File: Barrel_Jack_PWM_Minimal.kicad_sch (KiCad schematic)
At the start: 18 parts, among them J28 Barrel_Jack_Switch_Pin3Ring, J29 Barrel_Jack_Switch_Pin3Ring, J30 Barrel_Jack_Switch_Pin3Ring, J31 Barrel_Jack_Switch_Pin3Ring, J32 Barrel_Jack_Switch_Pin3Ring, J33 Barrel_Jack_Switch_Pin3Ring, J34 Barrel_Jack_Switch_Pin3Ring, J35 Barrel_Jack_Switch_Pin3Ring, U36 PCA9685PW

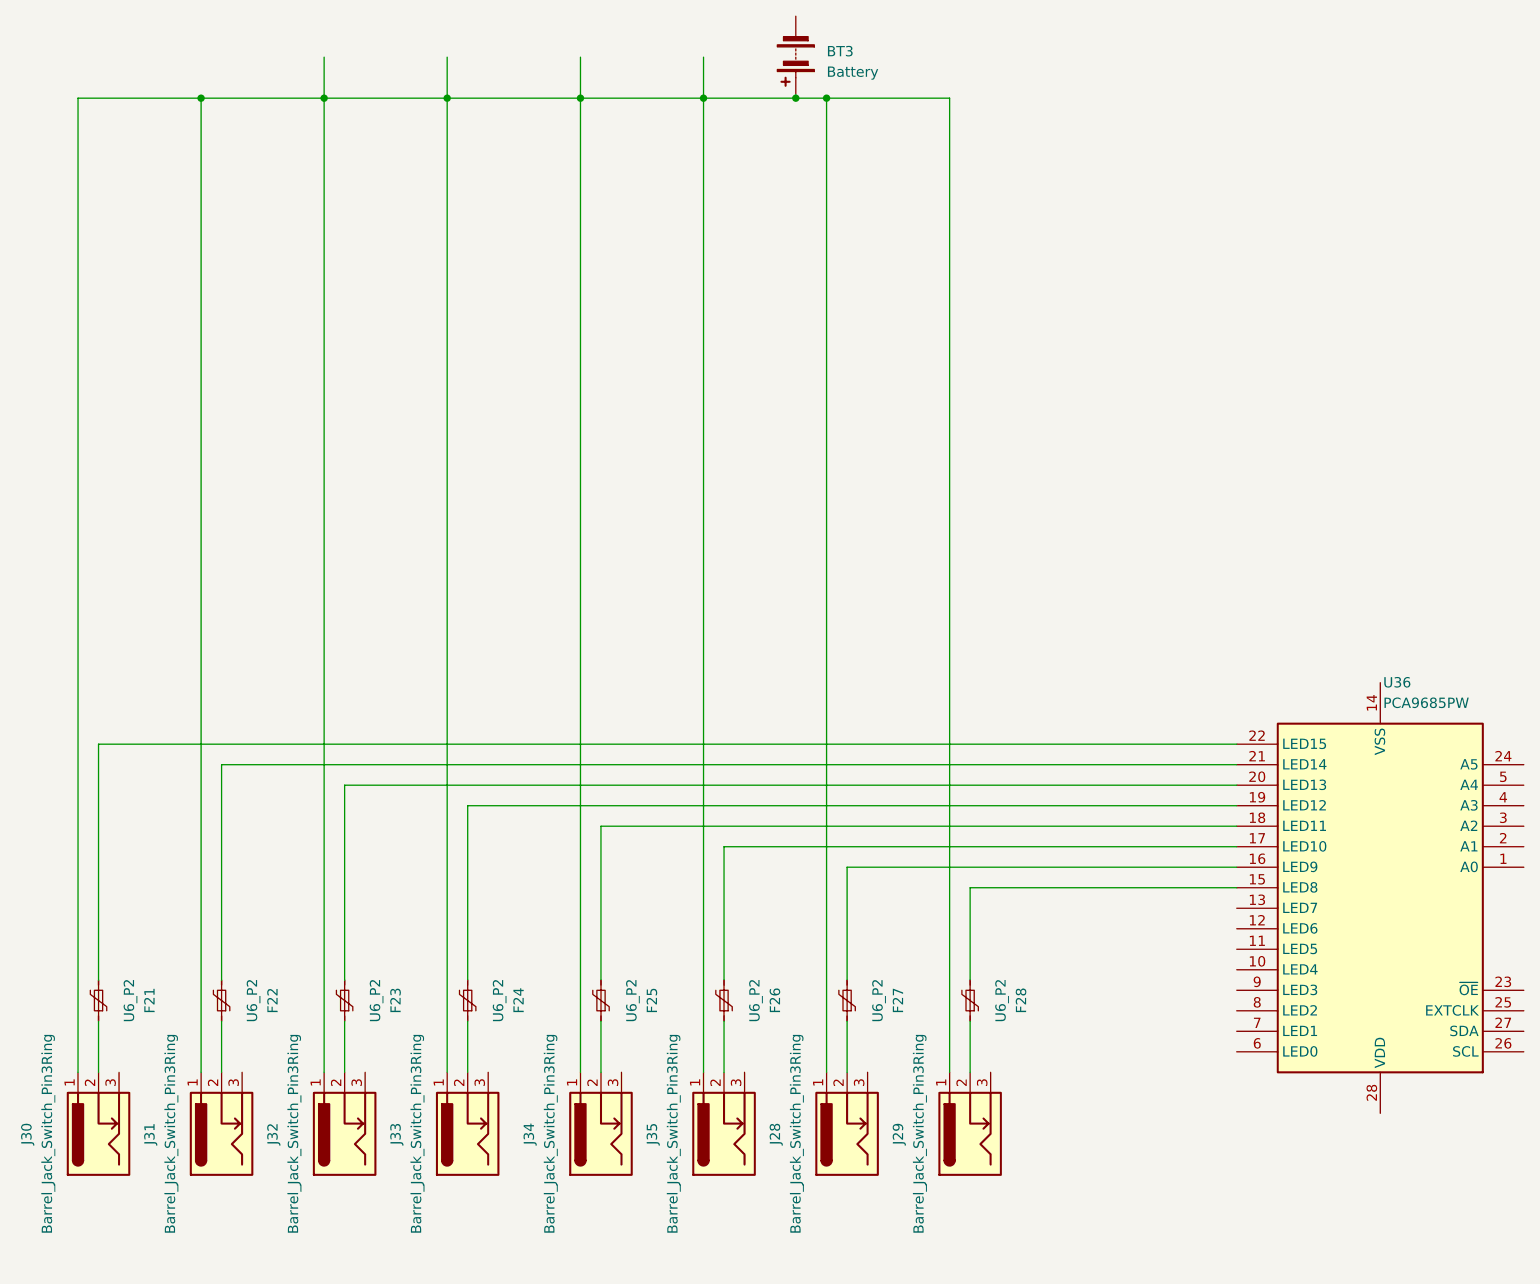
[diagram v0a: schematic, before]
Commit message: placeholders for ethernet and relay inputs
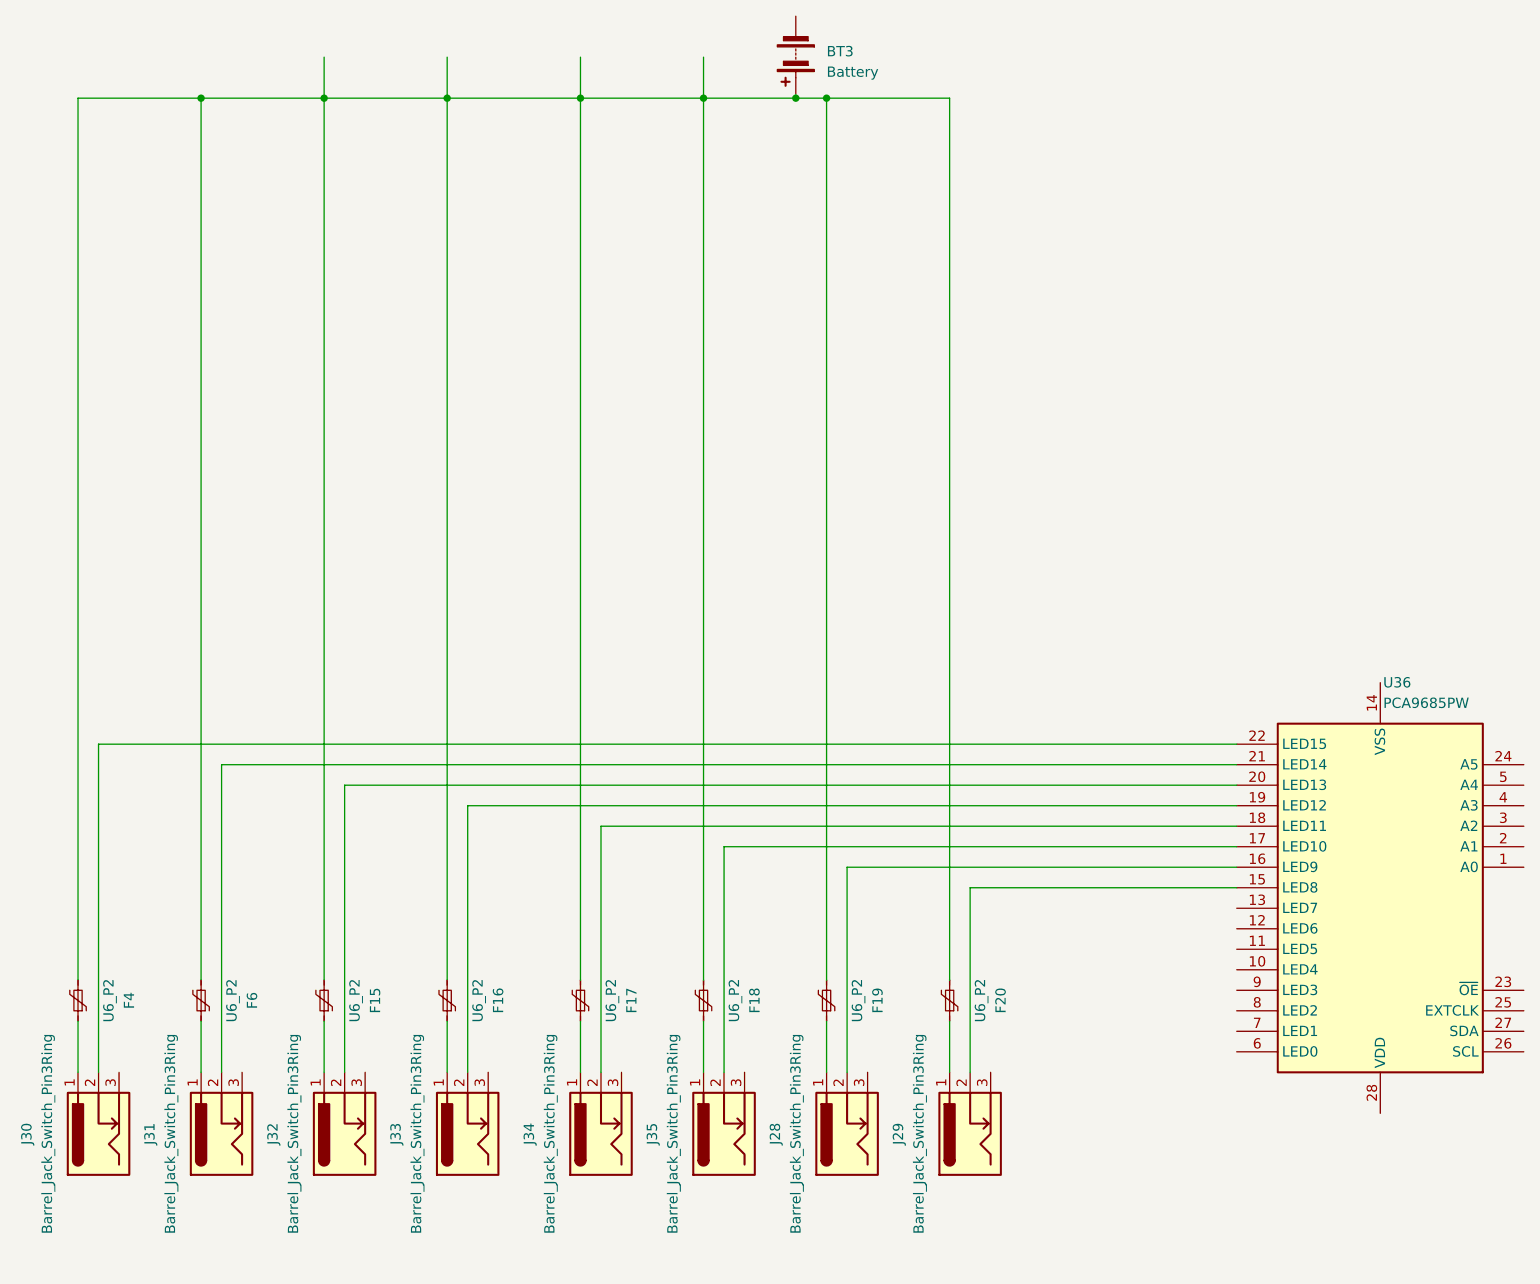
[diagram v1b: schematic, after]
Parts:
- removed F21, F22, F23, F24, F25, F26, F27, F28: U6_P2, symbol Device:Polyfuse_Small
- added F15, F16, F17, F18, F19, F20, F4, F6: U6_P2, symbol Device:Polyfuse_Small
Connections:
- net at J28.2: now also U36.16 (LED9)
- net at J32.2: now also U36.20 (LED13)
- net at J29.2: now also U36.15 (LED8)
- net at J35.2: now also U36.17 (LED10)
- net at J31.2: now also U36.21 (LED14)
- net at J34.2: now also U36.18 (LED11)
- net at U36.19 (LED12): now also J33.2
- net at U36.22 (LED15): now also J30.2
- new net: F19.1, J28.1
- new net: F17.1, J34.1
- new net: BT3.1 (+), F15.2, F16.2, F17.2, F18.2, F19.2, F20.2, F4.2, F6.2
- new net: F18.1, J35.1
- new net: F20.1, J29.1
- new net: F6.1, J31.1
- new net: F15.1, J32.1
- new net: F4.1, J30.1
- new net: F16.1, J33.1

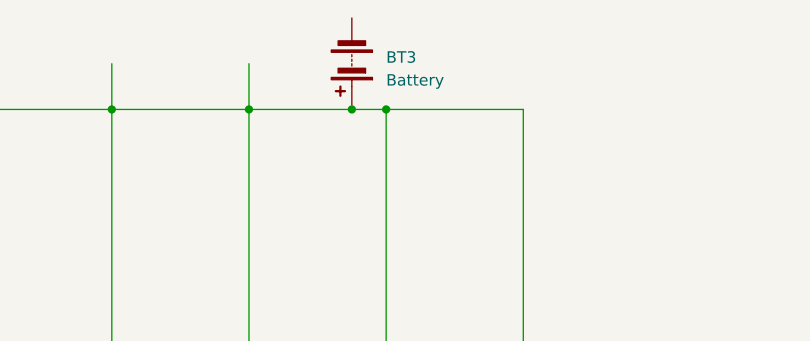
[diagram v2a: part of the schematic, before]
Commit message: PCB can be built, naming issues
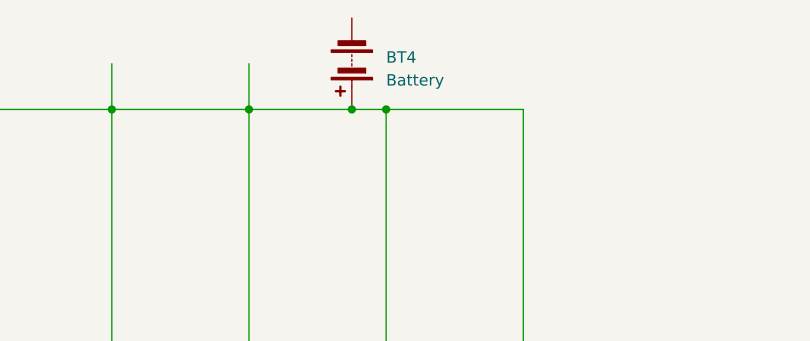
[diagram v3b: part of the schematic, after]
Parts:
- renumbered BT3 to BT4
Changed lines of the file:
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@@
   (symbol (lib_id "Device:Battery") (at 142.24 19.05 180) (unit 1)
     (in_bom yes) (on_board yes) (dnp no) (fields_autoplaced)
-    (property "Reference" "BT3" (at 146.05 18.3515 0)
+    (property "Reference" "BT4" (at 146.05 18.3515 0)
       (effects (font (size 1.27 1.27)) (justify right))
     )
@@
       (project "esp"
         (path "/dab6683c-420f-459a-bf9c-0c28b4b081e3/d534b787-d3bc-419e-b481-23d8b9503201/a1769b0b-efb6-4dd6-a1a8-a2cb27e19886"
-          (reference "BT3") (unit 1)
+          (reference "BT4") (unit 1)
         )
       )
